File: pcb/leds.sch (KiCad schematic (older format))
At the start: 15 parts

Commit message: Schematic version 1.0
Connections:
- net ENC_ext_LEDs renamed EXTERNAL_LEDS
- net LEDs_under_switches_DIN renamed AMBILIGHT_LEDS
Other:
- moved on the sheet: D?, J?

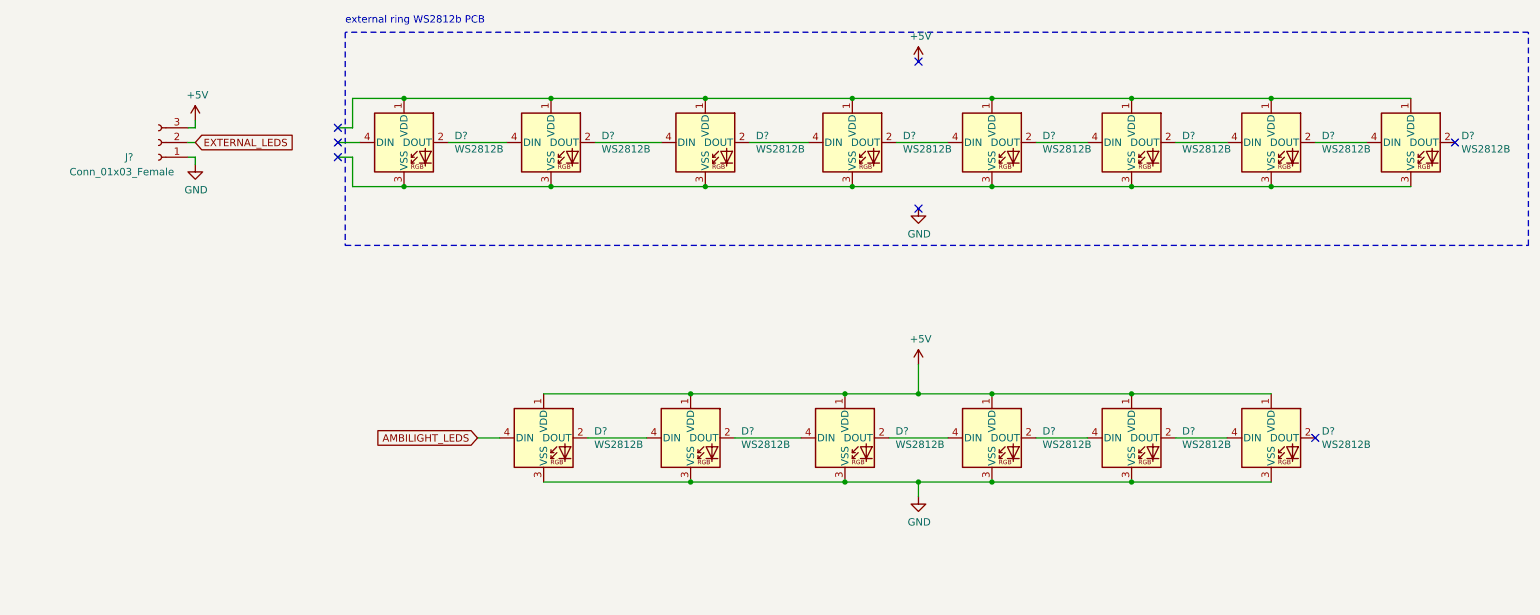
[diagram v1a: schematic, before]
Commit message: Added EEPROM memory & some footprints
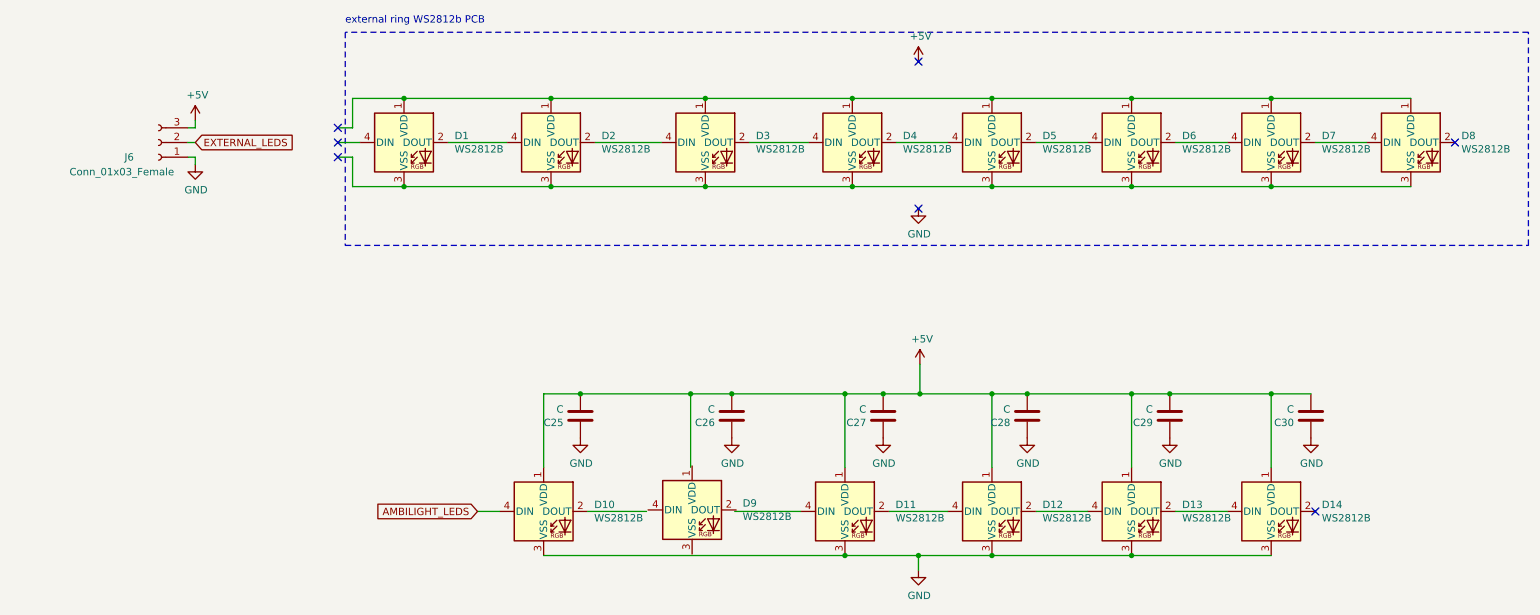
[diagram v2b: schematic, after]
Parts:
- added C25, C26, C27, C28, C29, C30: C, symbol Device:C
- J6: renamed from J?; footprint (none) -> Connector_PinHeader_2.54mm:PinHeader_1x03_P2.54mm_Vertical
- gave numbers to parts that had none: 14
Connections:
- wire segments 53 -> 66
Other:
- moved on the sheet: D10, D11, D12, D13, D14, D9

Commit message: Finish schematic and added footprints
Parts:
- C25, C26, C27, C28, C29, C30: footprint (none) -> Capacitor_SMD:C_0603_1608Metric
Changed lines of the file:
@@
 F 0 "C25" H 4405 3726 50  0000 L CNN
 F 1 "C" H 4405 3635 50  0000 L CNN
-F 2 "" H 4328 3530 50  0001 C CNN
+F 2 "Capacitor_SMD:C_0603_1608Metric" H 4328 3530 50  0001 C CNN
 F 3 "~" H 4290 3680 50  0001 C CNN
 	1    4290 3680
@@
 F 0 "C26" H 5435 3726 50  0000 L CNN
 F 1 "C" H 5435 3635 50  0000 L CNN
-F 2 "" H 5358 3530 50  0001 C CNN
+F 2 "Capacitor_SMD:C_0603_1608Metric" H 5358 3530 50  0001 C CNN
 F 3 "~" H 5320 3680 50  0001 C CNN
 	1    5320 3680
@@
 F 0 "C27" H 6465 3726 50  0000 L CNN
 F 1 "C" H 6465 3635 50  0000 L CNN
-F 2 "" H 6388 3530 50  0001 C CNN
+F 2 "Capacitor_SMD:C_0603_1608Metric" H 6388 3530 50  0001 C CNN
 F 3 "~" H 6350 3680 50  0001 C CNN
 	1    6350 3680
@@
 F 0 "C28" H 7445 3726 50  0000 L CNN
 F 1 "C" H 7445 3635 50  0000 L CNN
-F 2 "" H 7368 3530 50  0001 C CNN
+F 2 "Capacitor_SMD:C_0603_1608Metric" H 7368 3530 50  0001 C CNN
 F 3 "~" H 7330 3680 50  0001 C CNN
 	1    7330 3680
@@
 F 0 "C29" H 8415 3726 50  0000 L CNN
 F 1 "C" H 8415 3635 50  0000 L CNN
-F 2 "" H 8338 3530 50  0001 C CNN
+F 2 "Capacitor_SMD:C_0603_1608Metric" H 8338 3530 50  0001 C CNN
 F 3 "~" H 8300 3680 50  0001 C CNN
 	1    8300 3680
@@
 F 0 "C30" H 9375 3726 50  0000 L CNN
 F 1 "C" H 9375 3635 50  0000 L CNN
-F 2 "" H 9298 3530 50  0001 C CNN
+F 2 "Capacitor_SMD:C_0603_1608Metric" H 9298 3530 50  0001 C CNN
 F 3 "~" H 9260 3680 50  0001 C CNN
 	1    9260 3680

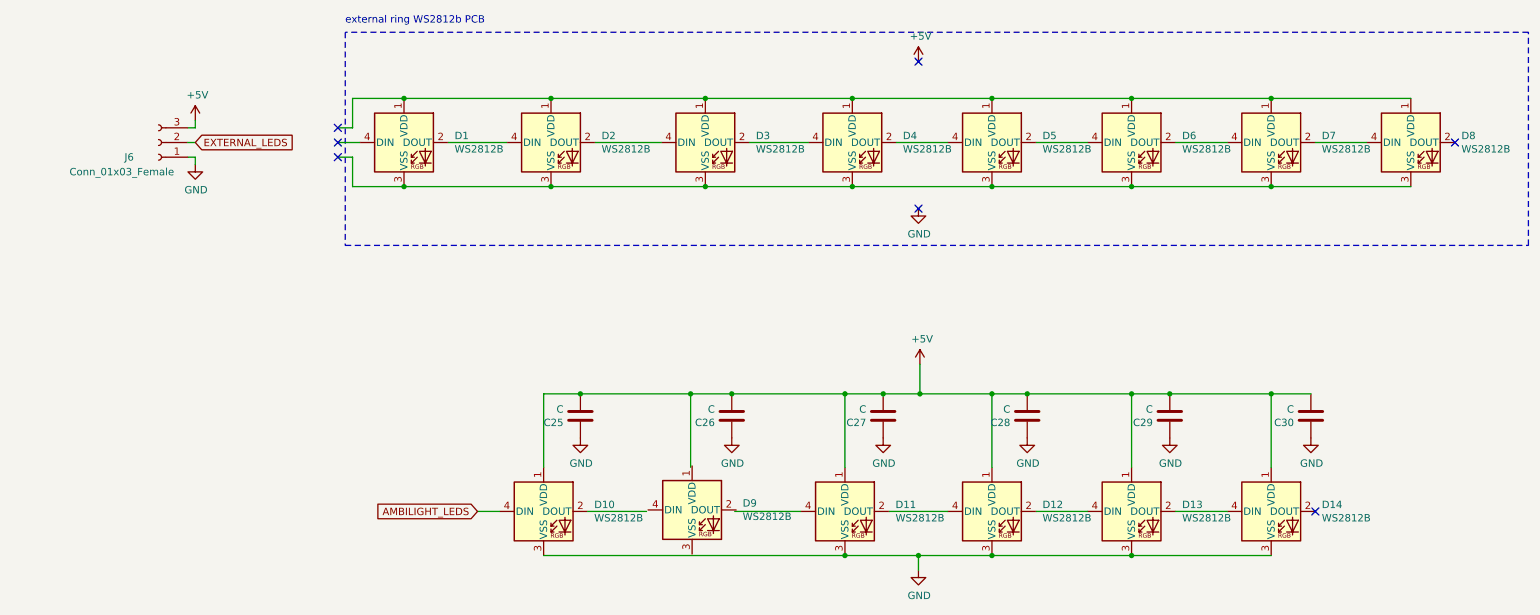
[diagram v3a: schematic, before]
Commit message: Footprints update and some changes
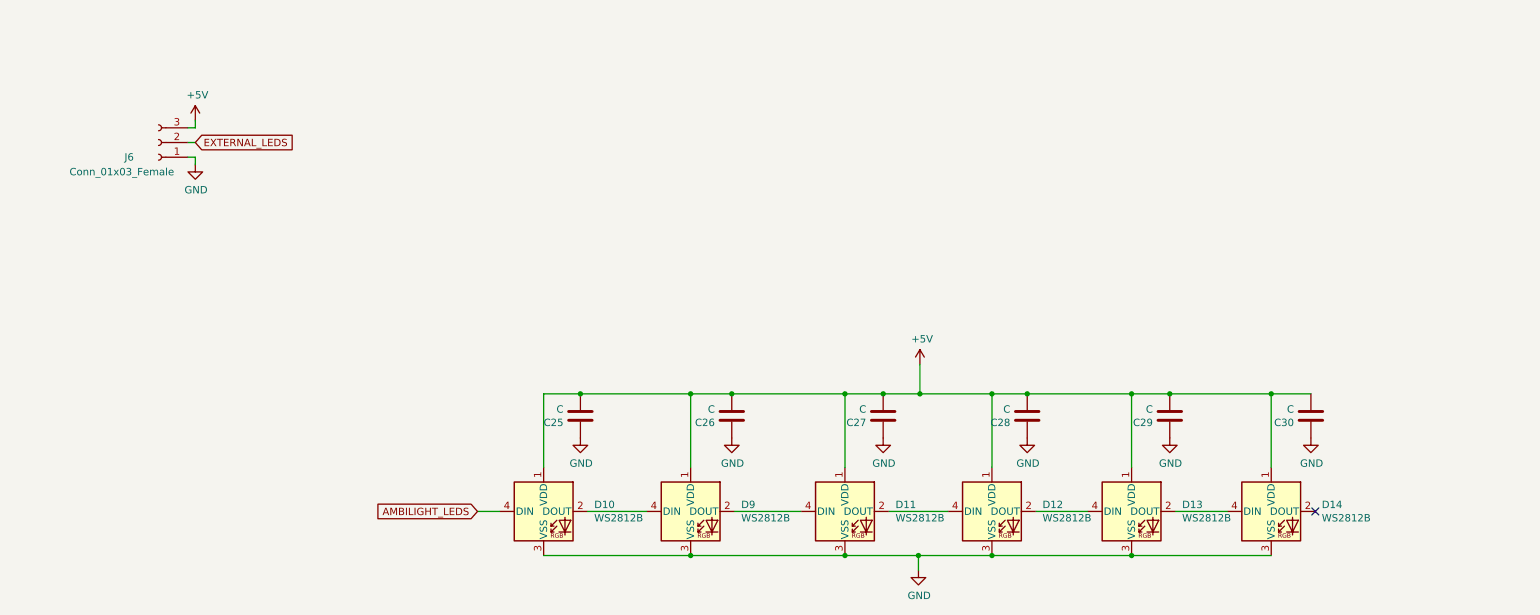
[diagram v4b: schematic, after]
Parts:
- removed D1, D2, D3, D4, D5, D6, D7, D8: WS2812B, LED_SMD:LED_WS2812B_PLCC4_5.0x5.0mm_P3.2mm, symbol LED:WS2812B
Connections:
- wire segments 66 -> 39
- no-connect marks 7 -> 1
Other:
- note removed: "external ring WS2812b PCB"
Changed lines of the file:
@@
 $EndDescr
-$Comp
-L LED:WS2812B D?
-U 1 1 61B5B747
-P 5140 1820
-AR Path="/61B5B747" Ref="D?"  Part="1"
-AR Path="/61B54BD1/61B5B747" Ref="D3"  Part="1"
-F 0 "D3" H 5484 1866 50  0000 L CNN
-F 1 "WS2812B" H 5484 1775 50  0000 L CNN
-F 2 "LED_SMD:LED_WS2812B_PLCC4_5.0x5.0mm_P3.2mm" H 5190 1520 50  0001 L TNN
-F 3 "https://cdn-shop.adafruit.com/datasheets/WS2812B.pdf" H 5240 1445 50  0001 L TNN
-	1    5140 1820
-	1    0    0    -1
-$EndComp
-$Comp
-L LED:WS2812B D?
-U 1 1 61B5B74D
-P 6140 1820
-AR Path="/61B5B74D" Ref="D?"  Part="1"
-AR Path="/61B54BD1/61B5B74D" Ref="D4"  Part="1"
-F 0 "D4" H 6484 1866 50  0000 L CNN
-F 1 "WS2812B" H 6484 1775 50  0000 L CNN
-F 2 "LED_SMD:LED_WS2812B_PLCC4_5.0x5.0mm_P3.2mm" H 6190 1520 50  0001 L TNN
-F 3 "https://cdn-shop.adafruit.com/datasheets/WS2812B.pdf" H 6240 1445 50  0001 L TNN
-	1    6140 1820
-	1    0    0    -1
-$EndComp
-$Comp
-L LED:WS2812B D?
-U 1 1 61B5B753
-P 7090 1820
-AR Path="/61B5B753" Ref="D?"  Part="1"
-AR Path="/61B54BD1/61B5B753" Ref="D5"  Part="1"
-F 0 "D5" H 7434 1866 50  0000 L CNN
-F 1 "WS2812B" H 7434 1775 50  0000 L CNN
-F 2 "LED_SMD:LED_WS2812B_PLCC4_5.0x5.0mm_P3.2mm" H 7140 1520 50  0001 L TNN
-F 3 "https://cdn-shop.adafruit.com/datasheets/WS2812B.pdf" H 7190 1445 50  0001 L TNN
-	1    7090 1820
-	1    0    0    -1
-$EndComp
-$Comp
-L LED:WS2812B D?
-U 1 1 61B5B759
-P 8040 1820
-AR Path="/61B5B759" Ref="D?"  Part="1"
-AR Path="/61B54BD1/61B5B759" Ref="D6"  Part="1"
-F 0 "D6" H 8384 1866 50  0000 L CNN
-F 1 "WS2812B" H 8384 1775 50  0000 L CNN
-F 2 "LED_SMD:LED_WS2812B_PLCC4_5.0x5.0mm_P3.2mm" H 8090 1520 50  0001 L TNN
-F 3 "https://cdn-shop.adafruit.com/datasheets/WS2812B.pdf" H 8140 1445 50  0001 L TNN
-	1    8040 1820
-	1    0    0    -1
-$EndComp
-$Comp
-L LED:WS2812B D?
-U 1 1 61B5B75F
-P 8990 1820
-AR Path="/61B5B75F" Ref="D?"  Part="1"
-AR Path="/61B54BD1/61B5B75F" Ref="D7"  Part="1"
-F 0 "D7" H 9334 1866 50  0000 L CNN
-F 1 "WS2812B" H 9334 1775 50  0000 L CNN
-F 2 "LED_SMD:LED_WS2812B_PLCC4_5.0x5.0mm_P3.2mm" H 9040 1520 50  0001 L TNN
-F 3 "https://cdn-shop.adafruit.com/datasheets/WS2812B.pdf" H 9090 1445 50  0001 L TNN
-	1    8990 1820
-	1    0    0    -1
-$EndComp
-$Comp
-L LED:WS2812B D?
-U 1 1 61B5B765
-P 9940 1820
-AR Path="/61B5B765" Ref="D?"  Part="1"
-AR Path="/61B54BD1/61B5B765" Ref="D8"  Part="1"
-F 0 "D8" H 10284 1866 50  0000 L CNN
-F 1 "WS2812B" H 10284 1775 50  0000 L CNN
-F 2 "LED_SMD:LED_WS2812B_PLCC4_5.0x5.0mm_P3.2mm" H 9990 1520 50  0001 L TNN
-F 3 "https://cdn-shop.adafruit.com/datasheets/WS2812B.pdf" H 10040 1445 50  0001 L TNN
-	1    9940 1820
-	1    0    0    -1
-$EndComp
-$Comp
-L LED:WS2812B D?
-U 1 1 61B5B76B
-P 3090 1820
-AR Path="/61B5B76B" Ref="D?"  Part="1"
-AR Path="/61B54BD1/61B5B76B" Ref="D1"  Part="1"
-F 0 "D1" H 3434 1866 50  0000 L CNN
-F 1 "WS2812B" H 3434 1775 50  0000 L CNN
-F 2 "LED_SMD:LED_WS2812B_PLCC4_5.0x5.0mm_P3.2mm" H 3140 1520 50  0001 L TNN
-F 3 "https://cdn-shop.adafruit.com/datasheets/WS2812B.pdf" H 3190 1445 50  0001 L TNN
-	1    3090 1820
-	1    0    0    -1
-$EndComp
-$Comp
-L LED:WS2812B D?
-U 1 1 61B5B771
-P 4090 1820
-AR Path="/61B5B771" Ref="D?"  Part="1"
-AR Path="/61B54BD1/61B5B771" Ref="D2"  Part="1"
-F 0 "D2" H 4434 1866 50  0000 L CNN
-F 1 "WS2812B" H 4434 1775 50  0000 L CNN
-F 2 "LED_SMD:LED_WS2812B_PLCC4_5.0x5.0mm_P3.2mm" H 4140 1520 50  0001 L TNN
-F 3 "https://cdn-shop.adafruit.com/datasheets/WS2812B.pdf" H 4190 1445 50  0001 L TNN
-	1    4090 1820
-	1    0    0    -1
-$EndComp
-Wire Wire Line
-	4090 1520 3090 1520
-Wire Wire Line
-	3090 2120 4090 2120
-Wire Wire Line
-	4090 1520 5140 1520
-Connection ~ 4090 1520
-Wire Wire Line
-	5140 1520 6140 1520
-Connection ~ 5140 1520
-Connection ~ 6140 1520
-Wire Wire Line
-	7090 1520 8040 1520
-Connection ~ 7090 1520
-Wire Wire Line
-	8040 1520 8990 1520
-Connection ~ 8040 1520
-Wire Wire Line
-	8990 1520 9940 1520
-Connection ~ 8990 1520
-Wire Wire Line
-	9940 2120 8990 2120
-Wire Wire Line
-	8990 2120 8040 2120
-Connection ~ 8990 2120
-Wire Wire Line
-	8040 2120 7090 2120
-Connection ~ 8040 2120
-Connection ~ 7090 2120
-Wire Wire Line
-	6140 2120 5140 2120
-Connection ~ 6140 2120
-Wire Wire Line
-	5140 2120 4090 2120
-Connection ~ 5140 2120
-Connection ~ 4090 2120
-$Comp
-L power:+5V #PWR?
-U 1 1 61B5B791
-P 6590 1270
-AR Path="/61B5B791" Ref="#PWR?"  Part="1"
-AR Path="/61B54BD1/61B5B791" Ref="#PWR075"  Part="1"
-F 0 "#PWR075" H 6590 1120 50  0001 C CNN
-F 1 "+5V" H 6605 1443 50  0000 C CNN
-F 2 "" H 6590 1270 50  0001 C CNN
-F 3 "" H 6590 1270 50  0001 C CNN
-	1    6590 1270
-	1    0    0    -1
-$EndComp
-$Comp
-L power:GND #PWR?
-U 1 1 61B5B79A
-P 6590 2270
-AR Path="/61B5B79A" Ref="#PWR?"  Part="1"
-AR Path="/61B54BD1/61B5B79A" Ref="#PWR078"  Part="1"
-F 0 "#PWR078" H 6590 2020 50  0001 C CNN
-F 1 "GND" H 6595 2097 50  0000 C CNN
-F 2 "" H 6590 2270 50  0001 C CNN
-F 3 "" H 6590 2270 50  0001 C CNN
-	1    6590 2270
-	1    0    0    -1
-$EndComp
-Wire Wire Line
-	3390 1820 3790 1820
-Wire Wire Line
-	4390 1820 4840 1820
-Wire Wire Line
-	5440 1820 5840 1820
-Wire Wire Line
-	6440 1820 6790 1820
-Wire Wire Line
-	7390 1820 7740 1820
-Wire Wire Line
-	8340 1820 8690 1820
-Wire Wire Line
-	9290 1820 9640 1820
-NoConn ~ 10240 1820
 $Comp
 L Connector:Conn_01x03_Female J?
@@
 	-1   0    0    1
 $EndComp
-Wire Wire Line
-	2640 1720 2740 1720
-Wire Wire Line
-	2740 1720 2740 1520
-Wire Wire Line
-	2740 1520 3090 1520
-Connection ~ 3090 1520
-Wire Wire Line
-	2640 1820 2790 1820
-Wire Wire Line
-	2640 1920 2740 1920
-Wire Wire Line
-	2740 1920 2740 2120
-Connection ~ 3090 2120
-Wire Wire Line
-	2740 2120 3090 2120
-Wire Notes Line
-	2690 2520 10740 2520
-Wire Notes Line
-	10740 2520 10740 1070
-Wire Notes Line
-	10740 1070 2690 1070
-Wire Notes Line
-	2690 1070 2690 2520
 $Comp
 L LED:WS2812B D?
@@
 L LED:WS2812B D?
 U 1 1 61B66E58
-P 5050 4320
+P 5040 4330
 AR Path="/61B66E58" Ref="D?"  Part="1"
 AR Path="/61B54BD1/61B66E58" Ref="D9"  Part="1"
-F 0 "D9" H 5394 4366 50  0000 L CNN
-F 1 "WS2812B" H 5394 4275 50  0000 L CNN
-F 2 "LED_SMD:LED_WS2812B_PLCC4_5.0x5.0mm_P3.2mm" H 5100 4020 50  0001 L TNN
-F 3 "https://cdn-shop.adafruit.com/datasheets/WS2812B.pdf" H 5150 3945 50  0001 L TNN
-	1    5050 4320
+F 0 "D9" H 5384 4376 50  0000 L CNN
+F 1 "WS2812B" H 5384 4285 50  0000 L CNN
+F 2 "LED_SMD:LED_WS2812B_PLCC4_5.0x5.0mm_P3.2mm" H 5090 4030 50  0001 L TNN
+F 3 "https://cdn-shop.adafruit.com/datasheets/WS2812B.pdf" H 5140 3955 50  0001 L TNN
+	1    5040 4330
 	1    0    0    -1
 $EndComp
@@
 	3590 4330 3740 4330
 NoConn ~ 9290 4330
-Text Notes 2690 1020 0    50   ~ 0
-external ring WS2812b PCB
 $Comp
 L LED:WS2812B D?
@@
 	1    0    0    -1
 $EndComp
-NoConn ~ 2640 1720
-NoConn ~ 2640 1820
-NoConn ~ 2640 1920
 $Comp
 L power:+5V #PWR076
@@
 Wire Wire Line
 	1620 1820 1670 1820
-Wire Wire Line
-	6140 1520 7090 1520
-NoConn ~ 6590 1270
-Wire Wire Line
-	6140 2120 7090 2120
-NoConn ~ 6590 2270
 Text GLabel 1670 1820 2    50   Input ~ 0
 EXTERNAL_LEDS
@@
 	5320 3530 6090 3530
 Wire Wire Line
-	4040 4630 6090 4630
+	4040 4630 5040 4630
 $Comp
 L Device:C C27
@@
 Wire Wire Line
 	7330 3530 8040 3530
+Connection ~ 5040 4630
+Wire Wire Line
+	5040 4630 6090 4630
 $EndSCHEMATC

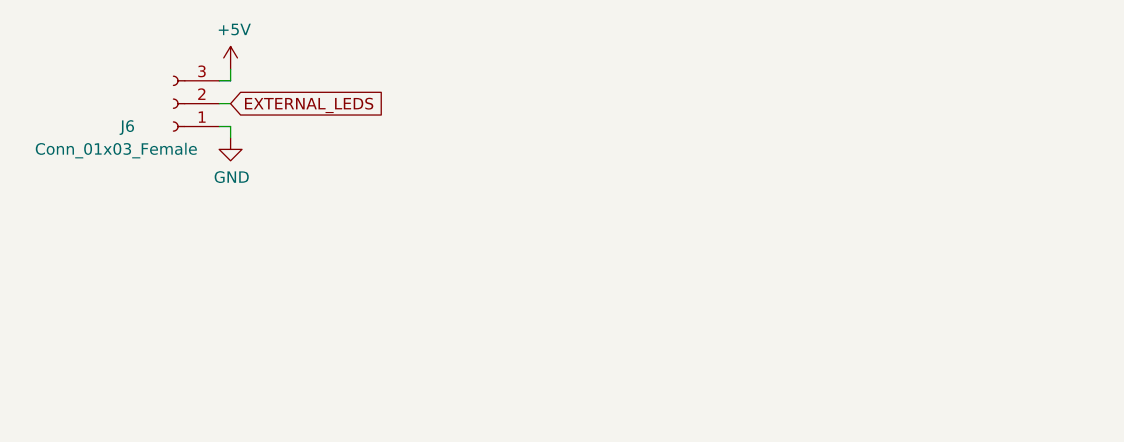
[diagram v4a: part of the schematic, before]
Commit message: Change connectors footprints
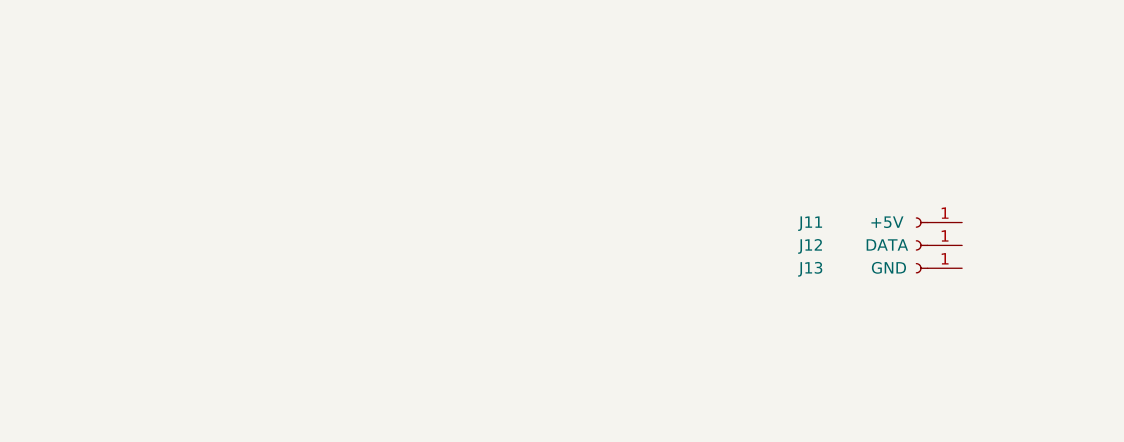
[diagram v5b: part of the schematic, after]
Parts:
- removed J6: Conn_01x03_Female, Connector_PinHeader_2.54mm:PinHeader_1x03_P2.54mm_Vertical, symbol Connector:Conn_01x03_Female
- added J11: +5V, TestPoint:TestPoint_Pad_D2.0mm, symbol Connector:Conn_01x01_Female
- added J12: DATA, TestPoint:TestPoint_Pad_D2.0mm, symbol Connector:Conn_01x01_Female
- added J13: GND, TestPoint:TestPoint_Pad_D2.0mm, symbol Connector:Conn_01x01_Female
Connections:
- net labels removed: EXTERNAL_LEDS
- wire segments 39 -> 34
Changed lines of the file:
@@
 $EndDescr
-$Comp
-L Connector:Conn_01x03_Female J?
-U 1 1 61B5B7AB
-P 1420 1820
-AR Path="/61B5B7AB" Ref="J?"  Part="1"
-AR Path="/61B54BD1/61B5B7AB" Ref="J6"  Part="1"
-F 0 "J6" H 1620 1920 50  0000 C CNN
-F 1 "Conn_01x03_Female" H 1670 2020 50  0000 C CNN
-F 2 "Connector_PinHeader_2.54mm:PinHeader_1x03_P2.54mm_Vertical" H 1420 1820 50  0001 C CNN
-F 3 "~" H 1420 1820 50  0001 C CNN
-	1    1420 1820
-	-1   0    0    1
-$EndComp
 $Comp
 L LED:WS2812B D?
@@
 	1    0    0    -1
 $EndComp
-$Comp
-L power:+5V #PWR076
-U 1 1 61B8D29A
-P 1670 1670
-F 0 "#PWR076" H 1670 1520 50  0001 C CNN
-F 1 "+5V" H 1685 1843 50  0000 C CNN
-F 2 "" H 1670 1670 50  0001 C CNN
-F 3 "" H 1670 1670 50  0001 C CNN
-	1    1670 1670
-	1    0    0    -1
-$EndComp
-$Comp
-L power:GND #PWR?
-U 1 1 61B8DECA
-P 1670 1970
-AR Path="/61B8DECA" Ref="#PWR?"  Part="1"
-AR Path="/61B54BD1/61B8DECA" Ref="#PWR077"  Part="1"
-F 0 "#PWR077" H 1670 1720 50  0001 C CNN
-F 1 "GND" H 1675 1797 50  0000 C CNN
-F 2 "" H 1670 1970 50  0001 C CNN
-F 3 "" H 1670 1970 50  0001 C CNN
-	1    1670 1970
-	1    0    0    -1
-$EndComp
-Wire Wire Line
-	1620 1720 1670 1720
-Wire Wire Line
-	1670 1720 1670 1670
-Wire Wire Line
-	1620 1920 1670 1920
-Wire Wire Line
-	1670 1920 1670 1970
-Wire Wire Line
-	1620 1820 1670 1820
-Text GLabel 1670 1820 2    50   Input ~ 0
-EXTERNAL_LEDS
 Text GLabel 3590 4330 0    50   Input ~ 0
 AMBILIGHT_LEDS
@@
 Wire Wire Line
 	5040 4630 6090 4630
+$Comp
+L Connector:Conn_01x01_Female J?
+U 1 1 61EFE4C5
+P 4670 2340
+AR Path="/61EFE4C5" Ref="J?"  Part="1"
+AR Path="/61B99CE8/61EFE4C5" Ref="J?"  Part="1"
+AR Path="/61B54BD1/61EFE4C5" Ref="J11"  Part="1"
+F 0 "J11" H 5130 2340 50  0000 C CNN
+F 1 "+5V" H 4800 2340 50  0000 C CNN
+F 2 "TestPoint:TestPoint_Pad_D2.0mm" H 4670 2340 50  0001 C CNN
+F 3 "~" H 4670 2340 50  0001 C CNN
+	1    4670 2340
+	-1   0    0    1
+$EndComp
+$Comp
+L Connector:Conn_01x01_Female J?
+U 1 1 61EFE4CB
+P 4670 2440
+AR Path="/61EFE4CB" Ref="J?"  Part="1"
+AR Path="/61B99CE8/61EFE4CB" Ref="J?"  Part="1"
+AR Path="/61B54BD1/61EFE4CB" Ref="J12"  Part="1"
+F 0 "J12" H 5130 2440 50  0000 C CNN
+F 1 "DATA" H 4800 2440 50  0000 C CNN
+F 2 "TestPoint:TestPoint_Pad_D2.0mm" H 4670 2440 50  0001 C CNN
+F 3 "~" H 4670 2440 50  0001 C CNN
+	1    4670 2440
+	-1   0    0    1
+$EndComp
+$Comp
+L Connector:Conn_01x01_Female J?
+U 1 1 61EFE4D1
+P 4670 2540
+AR Path="/61EFE4D1" Ref="J?"  Part="1"
+AR Path="/61B99CE8/61EFE4D1" Ref="J?"  Part="1"
+AR Path="/61B54BD1/61EFE4D1" Ref="J13"  Part="1"
+F 0 "J13" H 5130 2540 50  0000 C CNN
+F 1 "GND" H 4790 2540 50  0000 C CNN
+F 2 "TestPoint:TestPoint_Pad_D2.0mm" H 4670 2540 50  0001 C CNN
+F 3 "~" H 4670 2540 50  0001 C CNN
+	1    4670 2540
+	-1   0    0    1
+$EndComp
 $EndSCHEMATC
